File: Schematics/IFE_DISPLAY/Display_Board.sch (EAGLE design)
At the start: 20 parts, among them IC1 EP2C5T144, U1 EPCS1SI8N, U2 ATMEGA328P-AU

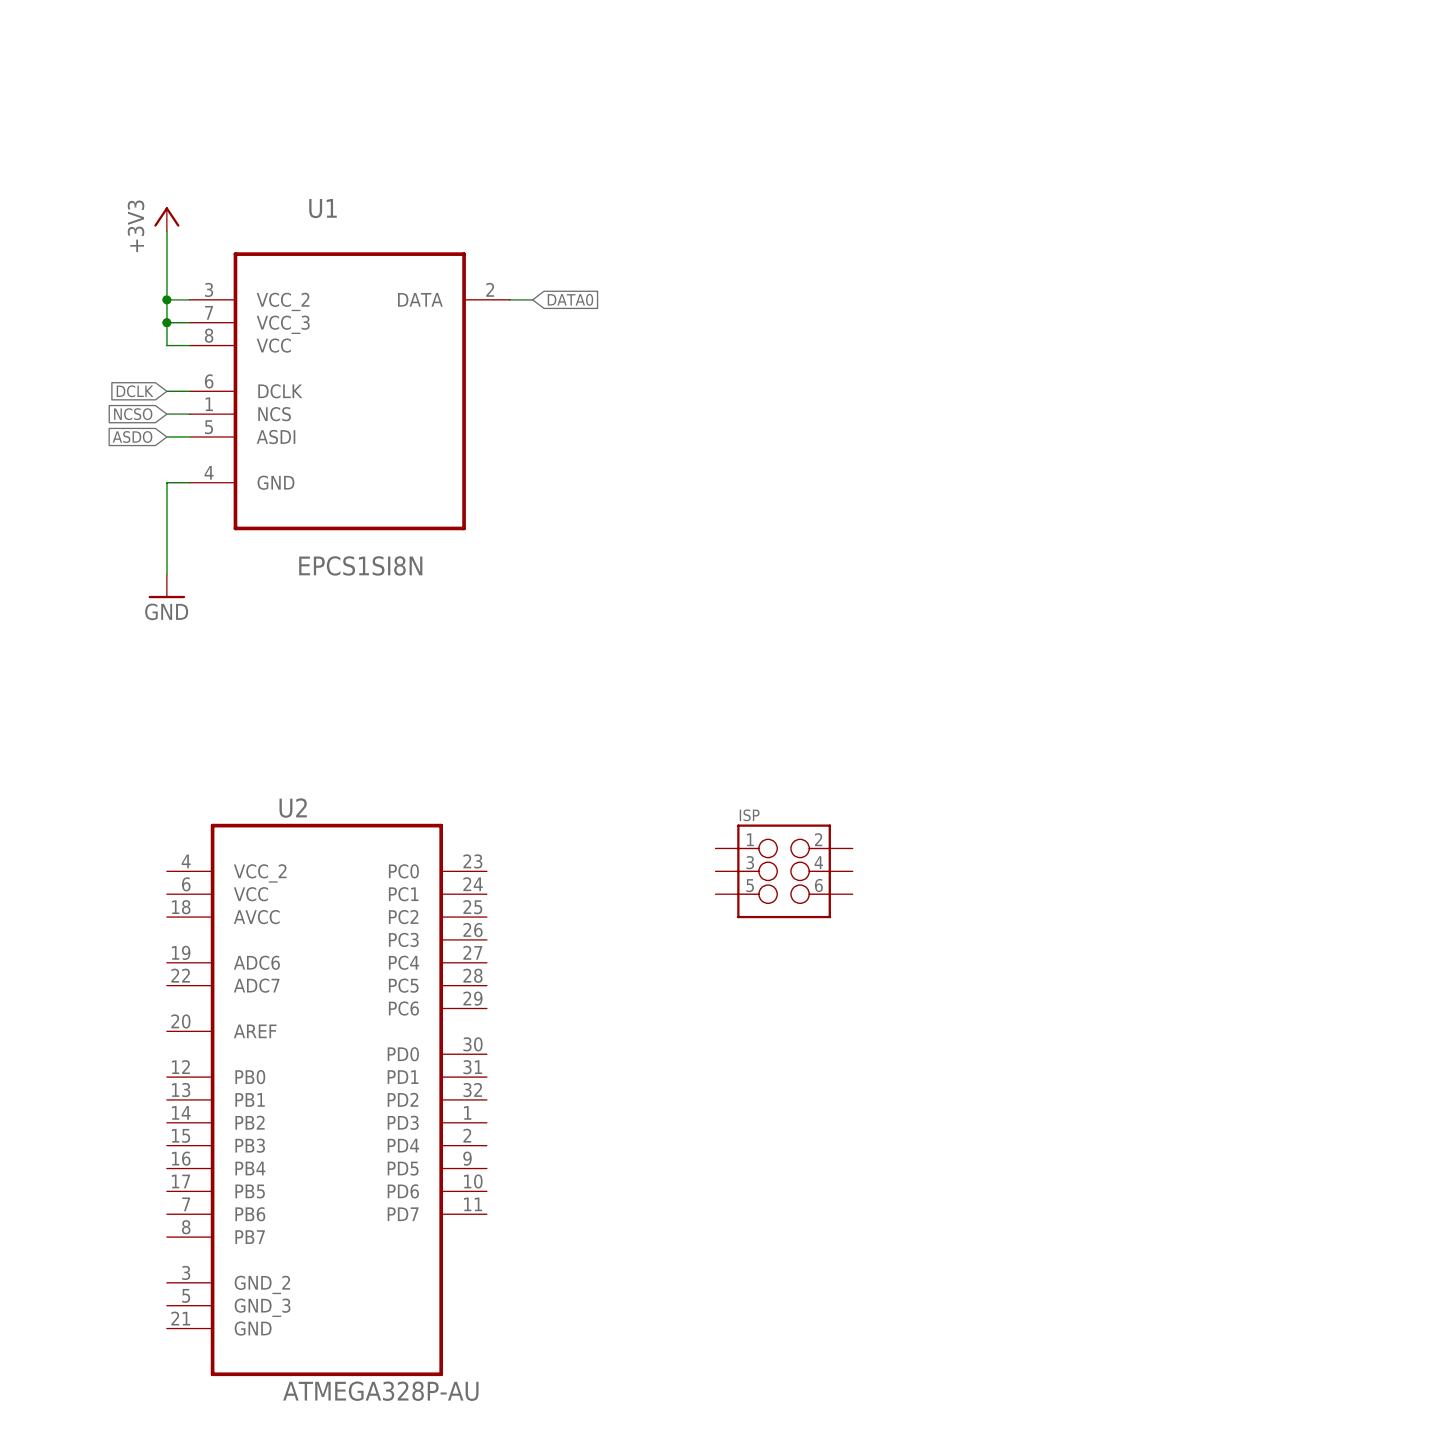
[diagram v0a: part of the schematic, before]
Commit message: Added Micro programmer circuit
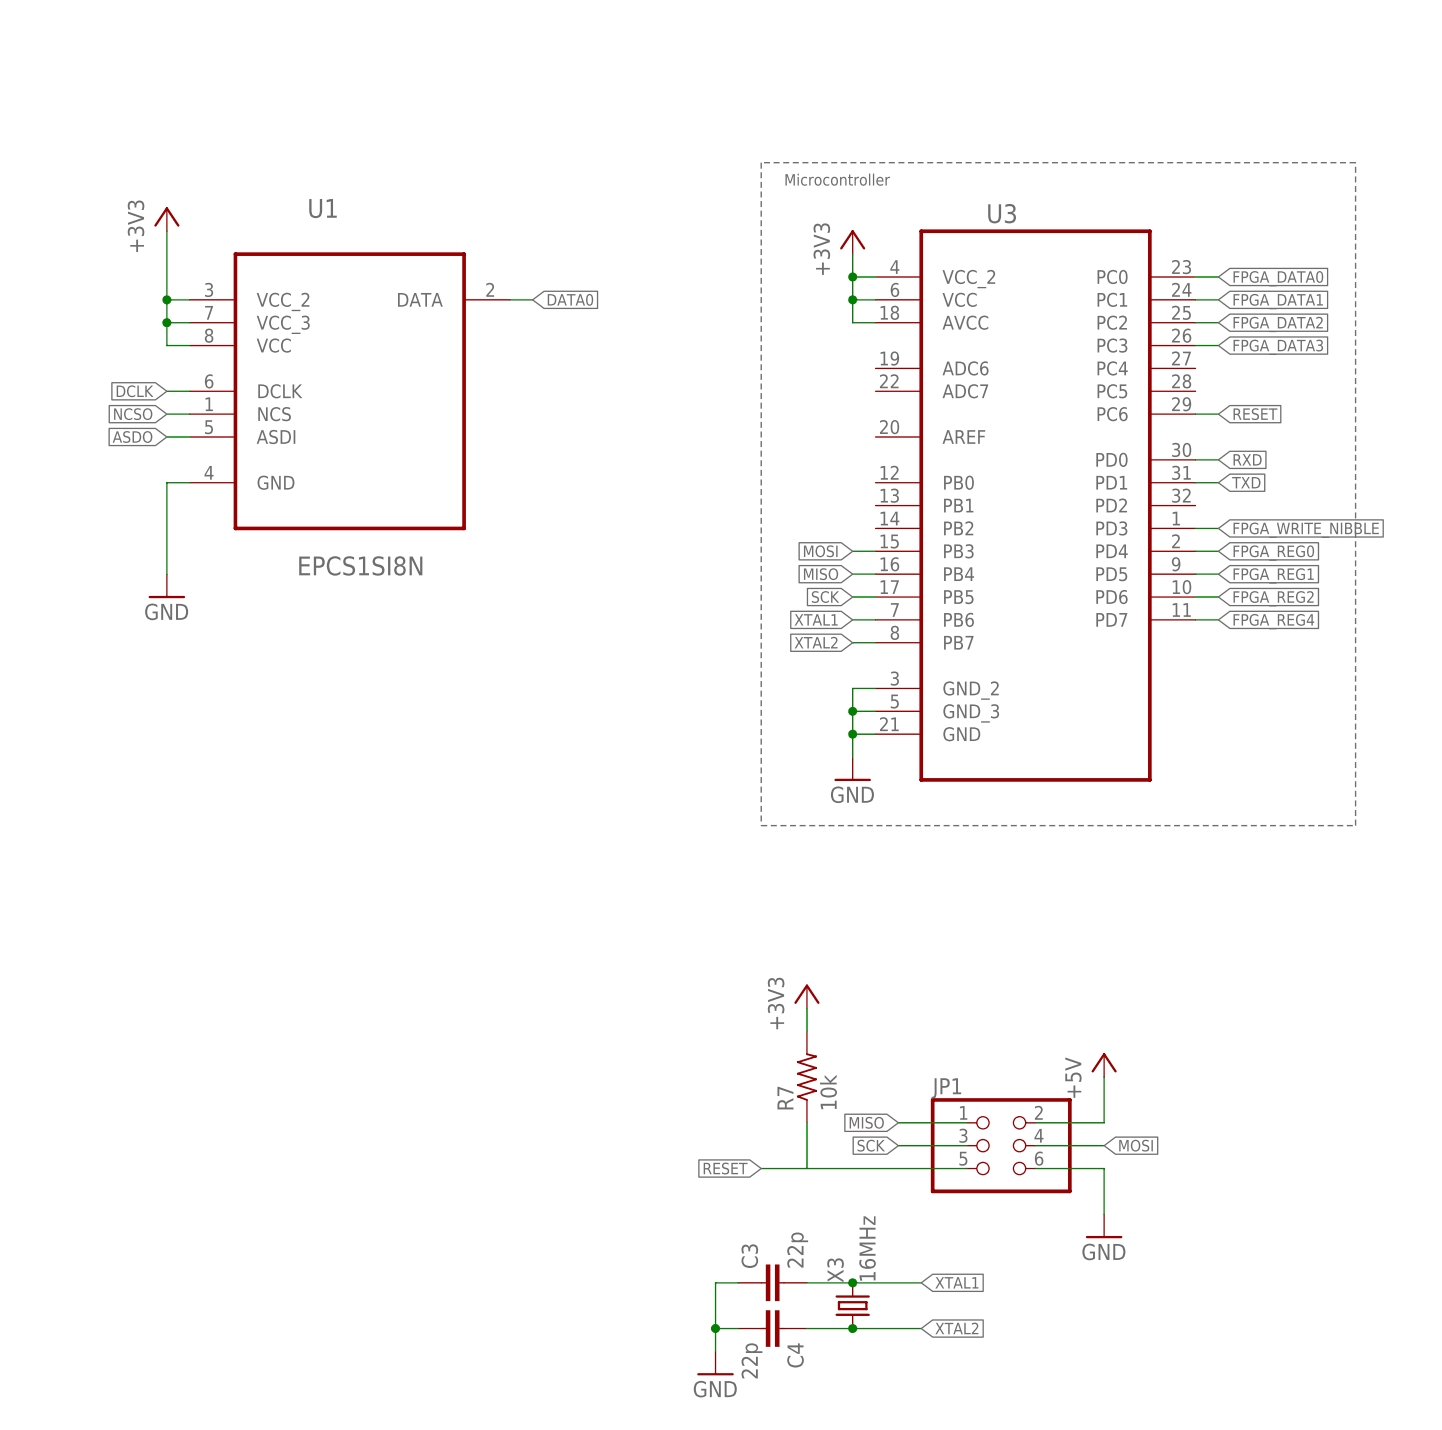
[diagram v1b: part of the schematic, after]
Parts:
- removed ISP: (no value), SparkFun-Connectors:M03X2NO_SILK
- removed U2: ATMEGA328P-AU, Atmel_By_element14_Batch_1-00:ATMEGA328P-AU
- added C3, C4: 22p, resistor:C-EUC0805K
- added JP1: (no value), pinhead:PINHD-2X3
- added R7: 10k, rcl:R-US_R0805
- added U3: ATMEGA328P-AU, Atmel_By_element14_Batch_1-00:ATMEGA328P-AU
- added X3: 16MHz, crystal:CRYSTAL
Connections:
- new net +5V: JP1.2
- new net FPGA_DATA0: U3.PC0
- new net FPGA_DATA1: U3.PC1
- new net FPGA_DATA2: U3.PC2
- new net FPGA_DATA3: U3.PC3
- new net FPGA_REG0: U3.PD4
- new net FPGA_REG1: U3.PD5
- new net FPGA_REG2: U3.PD6
- new net FPGA_REG4: U3.PD7
- new net FPGA_WRITE_NIBBLE: U3.PD3
- new net MISO: JP1.1, U3.PB4
- new net MOSI: JP1.4, U3.PB3
- new net RESET: JP1.5, R7.1, U3.PC6
- new net RXD: U3.PD0
- new net SCK: JP1.3, U3.PB5
- new net TXD: U3.PD1
- new net XTAL1: C3.2, U3.PB6, X3.2
- new net XTAL2: C4.1, U3.PB7, X3.1
- net +3V3: now also R7.2, U3.AVCC, U3.VCC, U3.VCC_2
- net GND: now also C3.1, C4.2, JP1.6, U3.GND, U3.GND_2, U3.GND_3
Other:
- note added: "Microcontroller"

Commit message: More work on Display Schematic
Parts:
- added C1: 0.1u, rcl:C-EUC0805K
- added C2: 0.22u, rcl:C-EUC0805K
- added C5: 220u, Capacitors:C1206
- added C6, C7: 22p, resistor:C-EUC0805K
- added C8, C9: 560p, rcl:C-EUC0805K
- added D1: PESD1CAN, diode:PESD1CAN
- added L2: 20uH, Inductors:MSS7348
- added Q1: 16MHz, adafruit:CRYSTALCTS406
- added R10: 4.7k, rcl:R-US_R0805
- added R8, R9: 100, rcl:R-US_R0805
- added U$2: MCP2515, Microchip_By_element14_Batch_1:MCP2515-I/SO
- added U$3: MCP2551, Microchip_By_element14_Batch_1:MCP2551-I/SN
- added U2: MX150_8_PIN, Connectors:MX150_8_PIN
- added U4, U5: HEX_CONVERTER, SparkFun-DigitalIC:HEX_CONVERTER
- added U6: MC7805BDD, IC's:MC7805BDD
- added WIFI_: (no value), Headers_IFE:PINHD-2X4
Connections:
- new net +12V: C2.1, C5.1, L2.2, U6.IN
- new net 2515_OSC1: C7.2, Q1.2, U$2.OSC1
- new net 2515_OSC2: C6.1, Q1.1, U$2.OSC2
- new net CANH: D1.1, R9.2, U$3.CANH
- new net CANL: D1.2, R8.2, U$3.CANL
- new net N$5: R10.2, U$3.RS
- new net N$6: C8.1, R8.1
- new net N$7: C9.1, R9.1
- new net PWR_IN: L2.1
- new net RXCAN: U$2.RXCAN, U$3.RXD
- new net TXCAN: U$2.TXCAN, U$3.TXD
- new net ~CS_CAN: U$2.~CS
- new net ~INT_CAN: U$2.~INT
- net +5V: now also C1.1, U$2.VDD, U$3.VDD, U6.OUT
- net GND: now also C1.2, C2.2, C5.2, C6.2, C7.1, C8.2, C9.2, D1.3, R10.1, U$2.VSS, U$3.VSS, U6.GND
- net MISO: now also U$2.SO
- net MOSI: now also U$2.SI
- net RESET: now also U$2.~RESET
- net SCK: now also U$2.SCK
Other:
- note added: "CAN Controller (MCP 2515)"
- note added: "CAN Tranciever (MCP 2551)"
- note added: "DC-DC Power Converter"
- moved on the sheet: LED1, LED2, LED3, R4, R5, R6, U1

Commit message: Figuring out power circuit
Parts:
- added C10, C11: 0.1u, rcl:C-EUC0805K
- added U$1: LM3940, Texas Instruments_By_element14_Batch_1:LM3940
- added U7: MCP1826S-1802E/DB, Microchip_By_element14_Batch_1:MCP1826S-1802E/DB
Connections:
- new net N$10: WIFI_.8
- new net N$8: WIFI_.1
- net +3V3: now also C10.1, U$1.VO, U7.VIN
- net +5V: now also U$1.VI
- net GND: now also C10.2, C11.2, U$1.GND, U7.GND_(TAB), U7.GND_(TAB)_2, WIFI_.2
- net VCC: now also C11.1, U7.VOUT
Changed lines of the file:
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@@
 <?xml version="1.0" encoding="utf-8"?>
 <!DOCTYPE eagle SYSTEM "eagle.dtd">
-<eagle version="8.3.1">
+<eagle version="8.1.1">
 <drawing>
 <settings>
 <setting alwaysvectorfont="no"/>
-<setting keepoldvectorfont="yes"/>
 <setting verticaltext="up"/>
 </settings>
@@
 <layers>
 <layer number="1" name="Top" color="4" fill="1" visible="no" active="no"/>
+<layer number="2" name="Route2" color="1" fill="3" visible="no" active="no"/>
+<layer number="3" name="Route3" color="4" fill="3" visible="no" active="no"/>
+<layer number="4" name="Route4" color="1" fill="4" visible="no" active="no"/>
+<layer number="5" name="Route5" color="4" fill="4" visible="no" active="no"/>
+<layer number="6" name="Route6" color="1" fill="8" visible="no" active="no"/>
+<layer number="7" name="Route7" color="4" fill="8" visible="no" active="no"/>
+<layer number="8" name="Route8" color="1" fill="2" visible="no" active="no"/>
+<layer number="9" name="Route9" color="4" fill="2" visible="no" active="no"/>
+<layer number="10" name="Route10" color="1" fill="7" visible="no" active="no"/>
+<layer number="11" name="Route11" color="4" fill="7" visible="no" active="no"/>
+<layer number="12" name="Route12" color="1" fill="5" visible="no" active="no"/>
+<layer number="13" name="Route13" color="4" fill="5" visible="no" active="no"/>
+<layer number="14" name="Route14" color="1" fill="6" visible="no" active="no"/>
+<layer number="15" name="Route15" color="4" fill="6" visible="no" active="no"/>
 <layer number="16" name="Bottom" color="1" fill="1" visible="no" active="no"/>
 <layer number="17" name="Pads" color="2" fill="1" visible="no" active="no"/>
@@
 <part name="R9" library="rcl" deviceset="R-US_" device="R0805" value="100"/>
 <part name="R10" library="rcl" deviceset="R-US_" device="R0805" value="4.7k"/>
+<part name="U$1" library="Texas Instruments_By_element14_Batch_1" deviceset="LM3940" device=""/>
+<part name="C10" library="rcl" deviceset="C-EU" device="C0805K" value="0.1u"/>
+<part name="GND20" library="supply1" deviceset="GND" device=""/>
+<part name="GND21" library="supply1" deviceset="GND" device=""/>
+<part name="+3V27" library="supply1" deviceset="+3V3" device=""/>
+<part name="U7" library="Microchip_By_element14_Batch_1" deviceset="MCP1826S-1802E/DB" device=""/>
+<part name="GND22" library="supply1" deviceset="GND" device=""/>
+<part name="P+11" library="supply1" deviceset="VCC" device="" value="1.2V"/>
+<part name="C11" library="rcl" deviceset="C-EU" device="C0805K" value="0.1u"/>
+<part name="GND23" library="supply1" deviceset="GND" device=""/>
+<part name="GND24" library="supply1" deviceset="GND" device=""/>
 </parts>
 <sheets>
@@
 <wire x1="307.34" y1="86.36" x2="241.3" y2="86.36" width="0.1524" layer="95" style="shortdash"/>
 <text x="243.84" y="83.82" size="1.27" layer="95">Microcontroller</text>
-<wire x1="297.18" y1="203.2" x2="411.48" y2="203.2" width="0.1524" layer="95" style="shortdash"/>
-<wire x1="411.48" y1="203.2" x2="411.48" y2="149.86" width="0.1524" layer="95" style="shortdash"/>
-<wire x1="411.48" y1="149.86" x2="297.18" y2="149.86" width="0.1524" layer="95" style="shortdash"/>
+<wire x1="297.18" y1="203.2" x2="482.6" y2="203.2" width="0.1524" layer="95" style="shortdash"/>
+<wire x1="482.6" y1="203.2" x2="482.6" y2="149.86" width="0.1524" layer="95" style="shortdash"/>
+<wire x1="482.6" y1="149.86" x2="297.18" y2="149.86" width="0.1524" layer="95" style="shortdash"/>
 <wire x1="297.18" y1="149.86" x2="297.18" y2="203.2" width="0.1524" layer="95" style="shortdash"/>
 <text x="299.72" y="200.66" size="1.27" layer="95">DC-DC Power Converter</text>
@@
 <instance part="R9" gate="G$1" x="492.76" y="-25.4" rot="R90"/>
 <instance part="R10" gate="G$1" x="419.1" y="-22.86" rot="R90"/>
+<instance part="U$1" gate="G$1" x="386.08" y="170.18"/>
+<instance part="C10" gate="G$1" x="403.86" y="165.1"/>
+<instance part="GND20" gate="1" x="403.86" y="154.94"/>
+<instance part="GND21" gate="1" x="386.08" y="154.94"/>
+<instance part="+3V27" gate="G$1" x="403.86" y="177.8"/>
+<instance part="U7" gate="A" x="436.88" y="170.18"/>
+<instance part="GND22" gate="1" x="411.48" y="154.94"/>
+<instance part="P+11" gate="VCC" x="467.36" y="172.72"/>
+<instance part="C11" gate="G$1" x="467.36" y="162.56"/>
+<instance part="GND23" gate="1" x="467.36" y="154.94"/>
+<instance part="GND24" gate="1" x="396.24" y="81.28"/>
 </instances>
 <busses>
@@
 <wire x1="487.68" y1="-45.72" x2="487.68" y2="-48.26" width="0.1524" layer="91"/>
 </segment>
+<segment>
+<pinref part="U$1" gate="G$1" pin="GND"/>
+<pinref part="GND21" gate="1" pin="GND"/>
+<wire x1="386.08" y1="162.56" x2="386.08" y2="157.48" width="0.1524" layer="91"/>
+</segment>
+<segment>
+<pinref part="C10" gate="G$1" pin="2"/>
+<pinref part="GND20" gate="1" pin="GND"/>
+<wire x1="403.86" y1="160.02" x2="403.86" y2="157.48" width="0.1524" layer="91"/>
+</segment>
+<segment>
+<pinref part="U7" gate="A" pin="GND_(TAB)"/>
+<wire x1="414.02" y1="165.1" x2="411.48" y2="165.1" width="0.1524" layer="91"/>
+<pinref part="GND22" gate="1" pin="GND"/>
+<wire x1="411.48" y1="165.1" x2="411.48" y2="162.56" width="0.1524" layer="91"/>
+<pinref part="U7" gate="A" pin="GND_(TAB)_2"/>
+<wire x1="411.48" y1="162.56" x2="411.48" y2="157.48" width="0.1524" layer="91"/>
+<wire x1="414.02" y1="162.56" x2="411.48" y2="162.56" width="0.1524" layer="91"/>
+<junction x="411.48" y="162.56"/>
+</segment>
+<segment>
+<pinref part="C11" gate="G$1" pin="2"/>
+<pinref part="GND23" gate="1" pin="GND"/>
+</segment>
+<segment>
+<pinref part="WIFI_" gate="A" pin="2"/>
+<wire x1="378.46" y1="83.82" x2="396.24" y2="83.82" width="0.1524" layer="91"/>
+<pinref part="GND24" gate="1" pin="GND"/>
+</segment>
 </net>
 <net name="+3V3" class="0">
@@
 <pinref part="+3V12" gate="G$1" pin="+3V3"/>
 </segment>
+<segment>
+<pinref part="U$1" gate="G$1" pin="VO"/>
+<wire x1="396.24" y1="170.18" x2="403.86" y2="170.18" width="0.1524" layer="91"/>
+<wire x1="403.86" y1="170.18" x2="403.86" y2="175.26" width="0.1524" layer="91"/>
+<wire x1="403.86" y1="170.18" x2="403.86" y2="167.64" width="0.1524" layer="91"/>
+<junction x="403.86" y="170.18"/>
+<pinref part="C10" gate="G$1" pin="1"/>
+<pinref part="+3V27" gate="G$1" pin="+3V3"/>
+<pinref part="U7" gate="A" pin="VIN"/>
+<wire x1="403.86" y1="170.18" x2="414.02" y2="170.18" width="0.1524" layer="91"/>
+</segment>
 </net>
 <net name="TDI" class="0">
@@
 <wire x1="109.22" y1="58.42" x2="121.92" y2="58.42" width="0.1524" layer="91"/>
 <pinref part="P+8" gate="VCC" pin="VCC"/>
+</segment>
+<segment>
+<pinref part="U7" gate="A" pin="VOUT"/>
+<wire x1="459.74" y1="165.1" x2="467.36" y2="165.1" width="0.1524" layer="91"/>
+<wire x1="467.36" y1="165.1" x2="467.36" y2="170.18" width="0.1524" layer="91"/>
+<pinref part="P+11" gate="VCC" pin="VCC"/>
+<pinref part="C11" gate="G$1" pin="1"/>
+<junction x="467.36" y="165.1"/>
 </segment>
 </net>
@@
 <junction x="368.3" y="170.18"/>
 <pinref part="U6" gate="G$1" pin="OUT"/>
+<pinref part="U$1" gate="G$1" pin="VI"/>
+<wire x1="368.3" y1="170.18" x2="375.92" y2="170.18" width="0.1524" layer="91"/>
 </segment>
 <segment>
@@
 </segment>
 </net>
+<net name="N$8" class="0">
+<segment>
+<pinref part="WIFI_" gate="A" pin="1"/>
+<wire x1="370.84" y1="83.82" x2="365.76" y2="83.82" width="0.1524" layer="91"/>
+</segment>
+</net>
+<net name="N$10" class="0">
+<segment>
+<pinref part="WIFI_" gate="A" pin="8"/>
+<wire x1="378.46" y1="76.2" x2="383.54" y2="76.2" width="0.1524" layer="91"/>
+</segment>
+</net>

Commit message: More progress on the schematic
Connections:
- removed net FPGA_REG4: U3.PD7
- removed net FPGA_WRITE_NIBBLE: U3.PD3
- removed net N$10: WIFI_.8
- removed net N$8: WIFI_.1
- new net BLUE_0: IC1.IO52
- new net BLUE_1: IC1.IO53
- new net BLUE_2: IC1.IO55
- new net BLUE_3: IC1.IO57
- new net BLUE_4: IC1.IO58
- new net BLUE_5: IC1.IO59
- new net BLUE_6: IC1.IO60
- new net BLUE_7: IC1.IO63
- new net FPGA_D0_3_3: IC1.IO142, U4.1Y
- new net FPGA_D1_3_3: IC1.IO141, U4.2Y
- new net FPGA_D2_3_3: IC1.IO139, U4.3Y
- new net FPGA_D3_3_3: IC1.IO137, U4.4Y
- new net FPGA_R0_3_3: IC1.IO136, U5.1Y
- new net FPGA_R1_3_3: IC1.IO135, U5.2Y
- new net FPGA_R2_3_3: IC1.IO134, U5.3Y
- new net FPGA_R3_3_3: IC1.IO133, U5.4Y
- new net FPGA_REG3: U3.PD7, U5.4A
- new net FPGA_REG_SEL: U3.PC4, U4.5A
- new net FPGA_RSEL_3_3: IC1.IO144, U4.5Y
- new net FPGA_WRITE: U3.PD3, U4.6A
- new net FPGA_W_3_3: IC1.IO143, U4.6Y
- new net GREEN_0: IC1.IO41
- new net GREEN_1: IC1.IO42
- new net GREEN_2: IC1.IO43
- new net GREEN_4: IC1.IO44
- new net GREEN_5: IC1.IO45
- new net GREEN_6: IC1.IO47
- new net GREEN_7: IC1.IO48
- new net GREEN_8: IC1.IO51
- new net RED_0: IC1.IO25
- new net RED_1: IC1.IO26
- new net RED_2: IC1.IO27
- new net RED_3: IC1.IO28
- new net RED_4: IC1.IO30
- new net RED_5: IC1.IO31
- new net RED_6: IC1.IO32
- new net RED_7: IC1.IO40
- new net TXD_3_3: U5.6Y, WIFI_.8
- net +3V3: now also U4.VCC, U5.VCC, WIFI_.3, WIFI_.5, WIFI_.7
- net CANH: now also U2.2
- net CANL: now also U2.1
- net FPGA_DATA0: now also U4.1A
- net FPGA_DATA1: now also U4.2A
- net FPGA_DATA2: now also U4.3A
- net FPGA_DATA3: now also U4.4A
- net FPGA_REG0: now also U5.1A
- net FPGA_REG1: now also U5.2A
- net FPGA_REG2: now also U5.3A
- net GND: now also U2.4, U4.GND, U5.GND
- net PWR_IN: now also U2.3
- net RXD: now also WIFI_.1
- net TXD: now also U5.6A
- net ~CS_CAN: now also U3.PC5
- net ~INT_CAN: now also U3.PD2
